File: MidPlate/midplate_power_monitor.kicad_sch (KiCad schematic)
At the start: 1 part, among them U3 LM2902

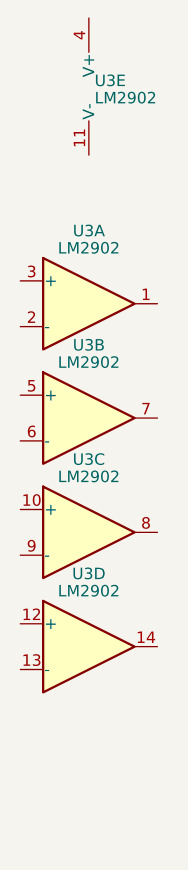
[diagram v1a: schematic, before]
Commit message: added switch and fuse
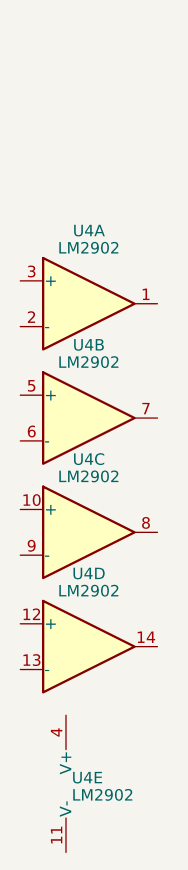
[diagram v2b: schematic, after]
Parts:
- renumbered U3 to U4
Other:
- moved on the sheet: U4E
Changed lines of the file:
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@@
   (symbol (lib_id "Amplifier_Operational:LM2902") (at 68.58 68.58 0) (unit 2)
     (in_bom yes) (on_board yes) (dnp no) (fields_autoplaced)
-    (property "Reference" "U3" (at 68.58 60.4901 0)
+    (property "Reference" "U4" (at 68.58 60.4901 0)
       (effects (font (size 1.27 1.27)))
     )
@@
       (project "midplate"
         (path "/69058343-dac8-421b-a3f6-e069eb1ba8ae/74030a08-2176-4dd5-aa31-e2ccc5e356bb"
-          (reference "U3") (unit 2)
+          (reference "U4") (unit 2)
         )
       )
@@
   (symbol (lib_id "Amplifier_Operational:LM2902") (at 68.58 55.88 0) (unit 1)
     (in_bom yes) (on_board yes) (dnp no) (fields_autoplaced)
-    (property "Reference" "U3" (at 68.58 47.7901 0)
+    (property "Reference" "U4" (at 68.58 47.7901 0)
       (effects (font (size 1.27 1.27)))
     )
@@
       (project "midplate"
         (path "/69058343-dac8-421b-a3f6-e069eb1ba8ae/74030a08-2176-4dd5-aa31-e2ccc5e356bb"
-          (reference "U3") (unit 1)
+          (reference "U4") (unit 1)
         )
       )
@@
   (symbol (lib_id "Amplifier_Operational:LM2902") (at 68.58 93.98 0) (unit 4)
     (in_bom yes) (on_board yes) (dnp no) (fields_autoplaced)
-    (property "Reference" "U3" (at 68.58 85.8901 0)
+    (property "Reference" "U4" (at 68.58 85.8901 0)
       (effects (font (size 1.27 1.27)))
     )
@@
       (project "midplate"
         (path "/69058343-dac8-421b-a3f6-e069eb1ba8ae/74030a08-2176-4dd5-aa31-e2ccc5e356bb"
-          (reference "U3") (unit 4)
+          (reference "U4") (unit 4)
         )
       )
@@
   (symbol (lib_id "Amplifier_Operational:LM2902") (at 68.58 81.28 0) (unit 3)
     (in_bom yes) (on_board yes) (dnp no) (fields_autoplaced)
-    (property "Reference" "U3" (at 68.58 73.1901 0)
+    (property "Reference" "U4" (at 68.58 73.1901 0)
       (effects (font (size 1.27 1.27)))
     )
@@
       (project "midplate"
         (path "/69058343-dac8-421b-a3f6-e069eb1ba8ae/74030a08-2176-4dd5-aa31-e2ccc5e356bb"
-          (reference "U3") (unit 3)
+          (reference "U4") (unit 3)
         )
       )
@@
     )
   )
-  (symbol (lib_id "Amplifier_Operational:LM2902") (at 71.12 31.75 0) (unit 5)
+  (symbol (lib_id "Amplifier_Operational:LM2902") (at 68.58 109.22 0) (unit 5)
     (in_bom yes) (on_board yes) (dnp no) (fields_autoplaced)
-    (property "Reference" "U3" (at 69.215 31.1063 0)
+    (property "Reference" "U4" (at 66.675 108.5763 0)
       (effects (font (size 1.27 1.27)) (justify left))
     )
-    (property "Value" "LM2902" (at 69.215 33.0273 0)
+    (property "Value" "LM2902" (at 66.675 110.4973 0)
       (effects (font (size 1.27 1.27)) (justify left))
     )
-    (property "Footprint" "Package_SO:SOIC-14_3.9x8.7mm_P1.27mm" (at 69.85 29.21 0)
+    (property "Footprint" "Package_SO:SOIC-14_3.9x8.7mm_P1.27mm" (at 67.31 106.68 0)
       (effects (font (size 1.27 1.27)) hide)
     )
-    (property "Datasheet" "http://www.ti.com/lit/ds/symlink/lm2902-n.pdf" (at 72.39 26.67 0)
+    (property "Datasheet" "http://www.ti.com/lit/ds/symlink/lm2902-n.pdf" (at 69.85 104.14 0)
       (effects (font (size 1.27 1.27)) hide)
     )
@@
       (project "midplate"
         (path "/69058343-dac8-421b-a3f6-e069eb1ba8ae/74030a08-2176-4dd5-aa31-e2ccc5e356bb"
-          (reference "U3") (unit 5)
+          (reference "U4") (unit 5)
         )
       )

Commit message: powerboard HV powerpillars + midplate
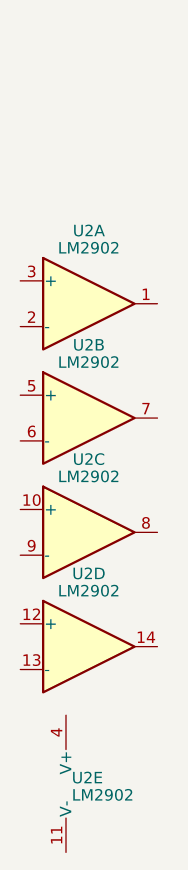
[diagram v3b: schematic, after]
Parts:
- renumbered U4 to U2
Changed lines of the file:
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@@
   (symbol (lib_id "Amplifier_Operational:LM2902") (at 68.58 68.58 0) (unit 2)
     (in_bom yes) (on_board yes) (dnp no) (fields_autoplaced)
-    (property "Reference" "U4" (at 68.58 60.4901 0)
+    (property "Reference" "U2" (at 68.58 60.4901 0)
       (effects (font (size 1.27 1.27)))
     )
@@
       (project "midplate"
         (path "/69058343-dac8-421b-a3f6-e069eb1ba8ae/74030a08-2176-4dd5-aa31-e2ccc5e356bb"
-          (reference "U4") (unit 2)
+          (reference "U2") (unit 2)
         )
       )
@@
   (symbol (lib_id "Amplifier_Operational:LM2902") (at 68.58 55.88 0) (unit 1)
     (in_bom yes) (on_board yes) (dnp no) (fields_autoplaced)
-    (property "Reference" "U4" (at 68.58 47.7901 0)
+    (property "Reference" "U2" (at 68.58 47.7901 0)
       (effects (font (size 1.27 1.27)))
     )
@@
       (project "midplate"
         (path "/69058343-dac8-421b-a3f6-e069eb1ba8ae/74030a08-2176-4dd5-aa31-e2ccc5e356bb"
-          (reference "U4") (unit 1)
+          (reference "U2") (unit 1)
         )
       )
@@
   (symbol (lib_id "Amplifier_Operational:LM2902") (at 68.58 93.98 0) (unit 4)
     (in_bom yes) (on_board yes) (dnp no) (fields_autoplaced)
-    (property "Reference" "U4" (at 68.58 85.8901 0)
+    (property "Reference" "U2" (at 68.58 85.8901 0)
       (effects (font (size 1.27 1.27)))
     )
@@
       (project "midplate"
         (path "/69058343-dac8-421b-a3f6-e069eb1ba8ae/74030a08-2176-4dd5-aa31-e2ccc5e356bb"
-          (reference "U4") (unit 4)
+          (reference "U2") (unit 4)
         )
       )
@@
   (symbol (lib_id "Amplifier_Operational:LM2902") (at 68.58 81.28 0) (unit 3)
     (in_bom yes) (on_board yes) (dnp no) (fields_autoplaced)
-    (property "Reference" "U4" (at 68.58 73.1901 0)
+    (property "Reference" "U2" (at 68.58 73.1901 0)
       (effects (font (size 1.27 1.27)))
     )
@@
       (project "midplate"
         (path "/69058343-dac8-421b-a3f6-e069eb1ba8ae/74030a08-2176-4dd5-aa31-e2ccc5e356bb"
-          (reference "U4") (unit 3)
+          (reference "U2") (unit 3)
         )
       )
@@
   (symbol (lib_id "Amplifier_Operational:LM2902") (at 68.58 109.22 0) (unit 5)
     (in_bom yes) (on_board yes) (dnp no) (fields_autoplaced)
-    (property "Reference" "U4" (at 66.675 108.5763 0)
+    (property "Reference" "U2" (at 66.675 108.5763 0)
       (effects (font (size 1.27 1.27)) (justify left))
     )
@@
       (project "midplate"
         (path "/69058343-dac8-421b-a3f6-e069eb1ba8ae/74030a08-2176-4dd5-aa31-e2ccc5e356bb"
-          (reference "U4") (unit 5)
+          (reference "U2") (unit 5)
         )
       )
